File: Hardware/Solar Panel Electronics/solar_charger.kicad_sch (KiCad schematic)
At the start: 30 parts, among them J1 Screw_Terminal_SolarPanel_Inp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, U3 LT3652EDD, U4 LTC4411ES5TRMPBF

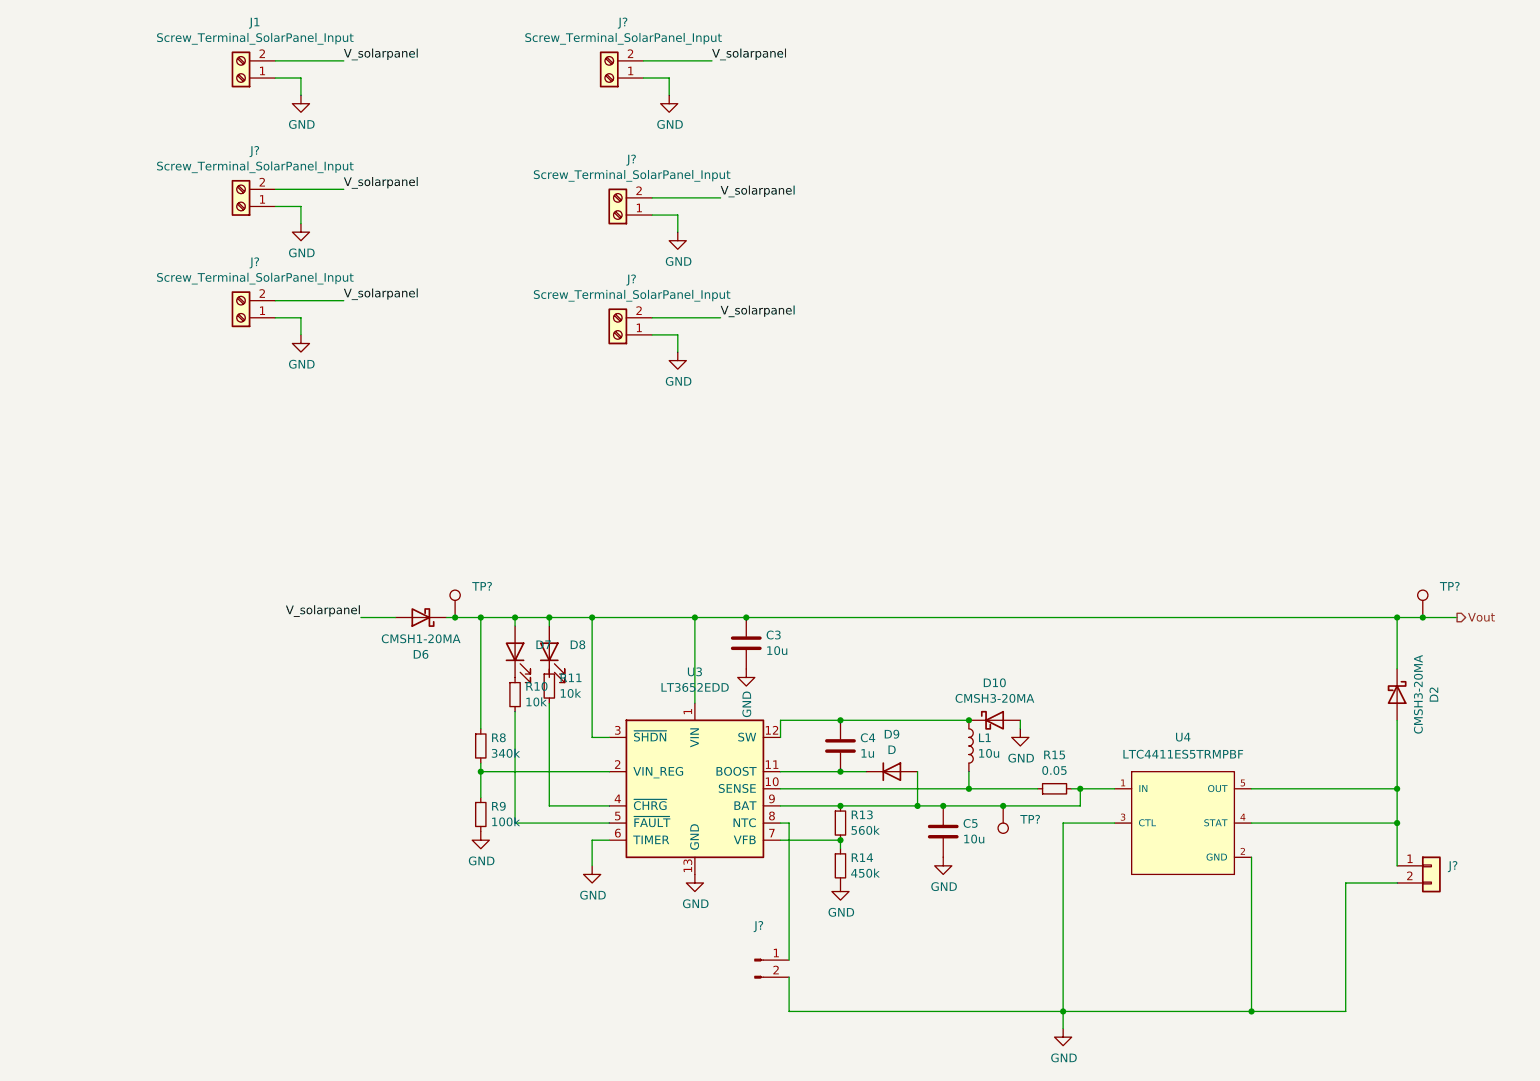
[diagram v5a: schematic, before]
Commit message: Added power measuring circuitry using potential dividers. Needs to be double checked
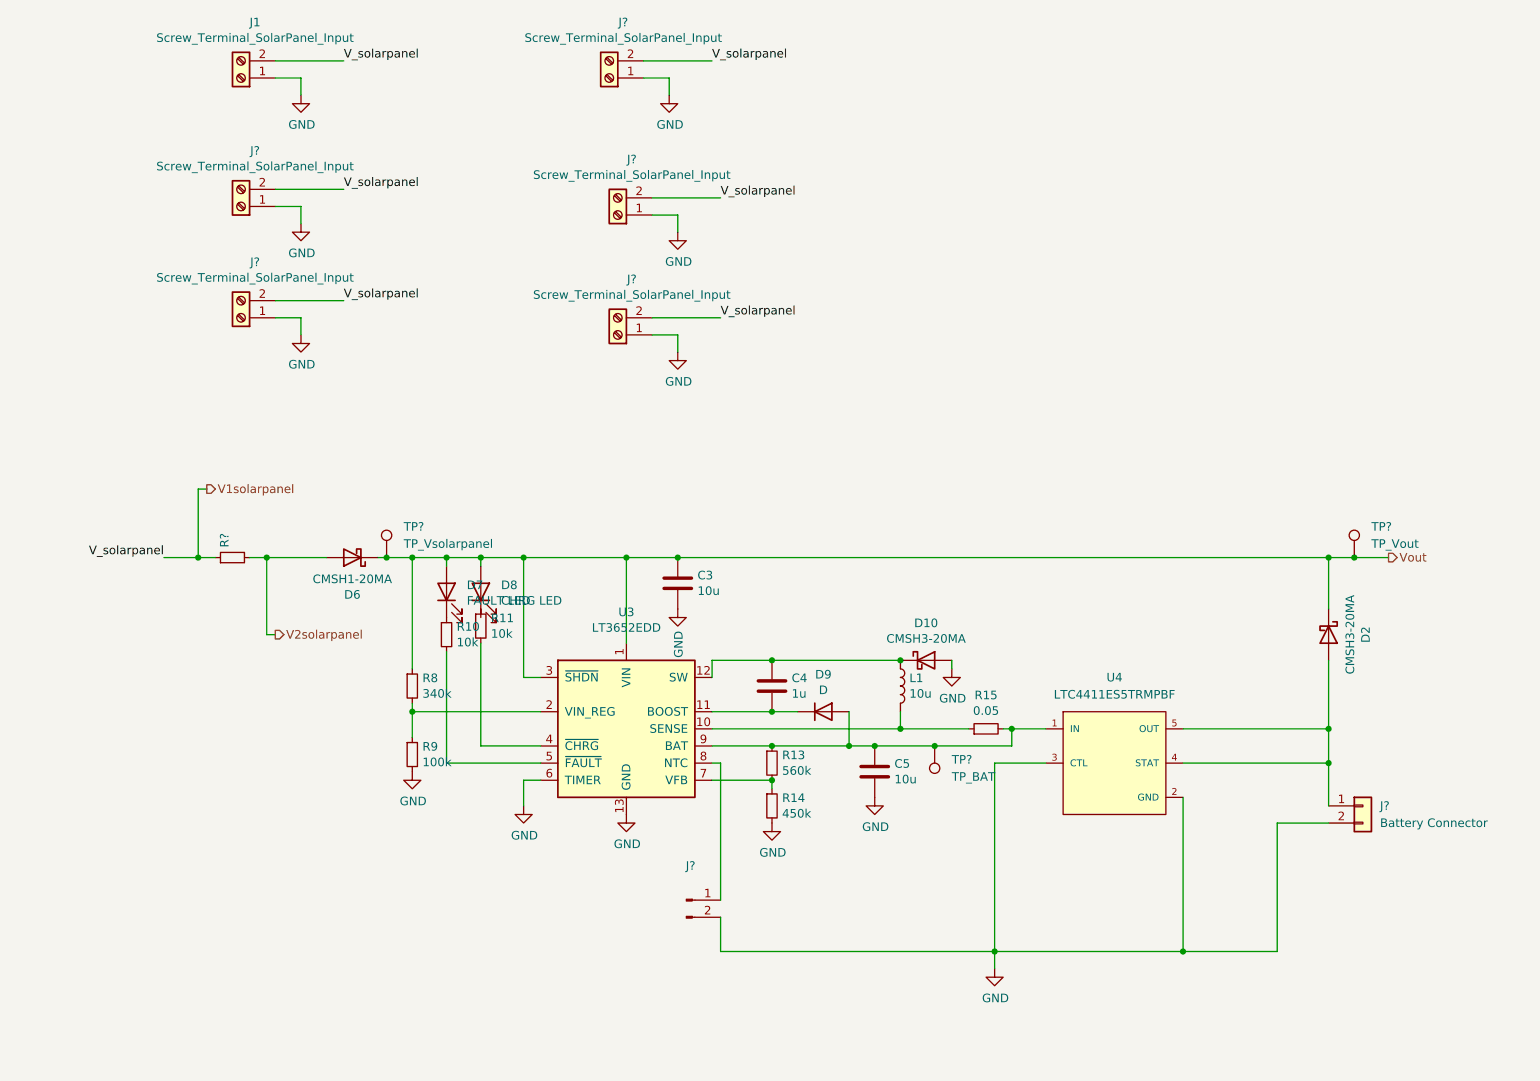
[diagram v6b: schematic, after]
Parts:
- added R?: (no value), symbol Device:R_Small
- D7: value (none) -> FAULT LED
- D8: value (none) -> CHRG LED
- J?: value (none) -> Battery Connector; footprint (none) -> Connector_JST:JST_ACH_BM02B-ACHSS-GAN-ETF_1x02-1MP_P1.20mm_Vertical
- TP?: value (none) -> TP_BAT
- TP?: value (none) -> TP_Vout
- TP?: value (none) -> TP_Vsolarpanel
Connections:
- net V_solarpanel renamed V1solarpanel
- net V1solarpanel: now also R?.1; no longer D6.2 (A)
- new net V2solarpanel: D6.2 (A), R?.2
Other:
- moved on the sheet: C3, C4, C5, D10, D2, D6, D7, D8, D9, J?, L1, R10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

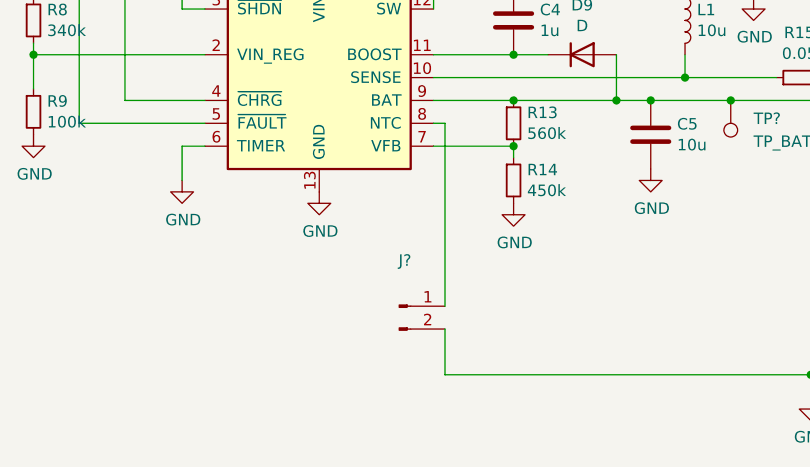
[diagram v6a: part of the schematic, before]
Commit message: Added voltage regulators. Need to size components
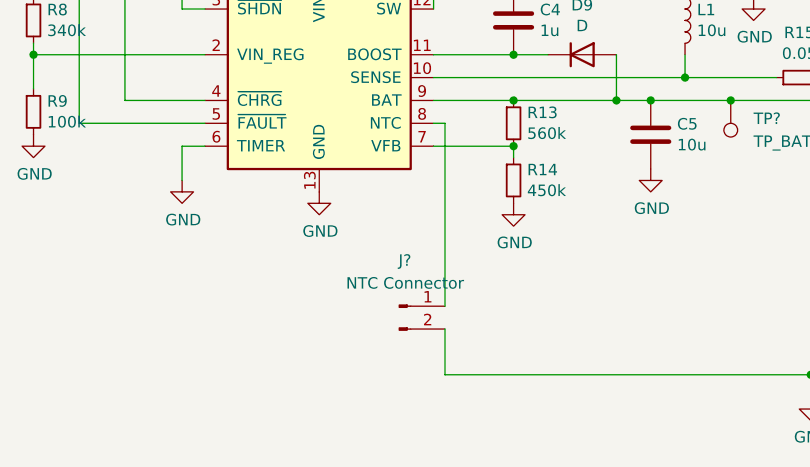
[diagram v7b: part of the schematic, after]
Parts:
- J?: value (none) -> NTC Connector
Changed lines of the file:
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@@
     (in_bom yes) (on_board yes) (fields_autoplaced)
     (property "Reference" "J?" (id 0) (at 114.935 140.97 0))
-    (property "Value" "" (id 1) (at 114.935 143.51 0))
+    (property "Value" "NTC Connector" (id 1) (at 114.935 143.51 0))
     (property "Footprint" "" (id 2) (at 114.3 146.05 0)
       (effects (font (size 1.27 1.27)) hide)

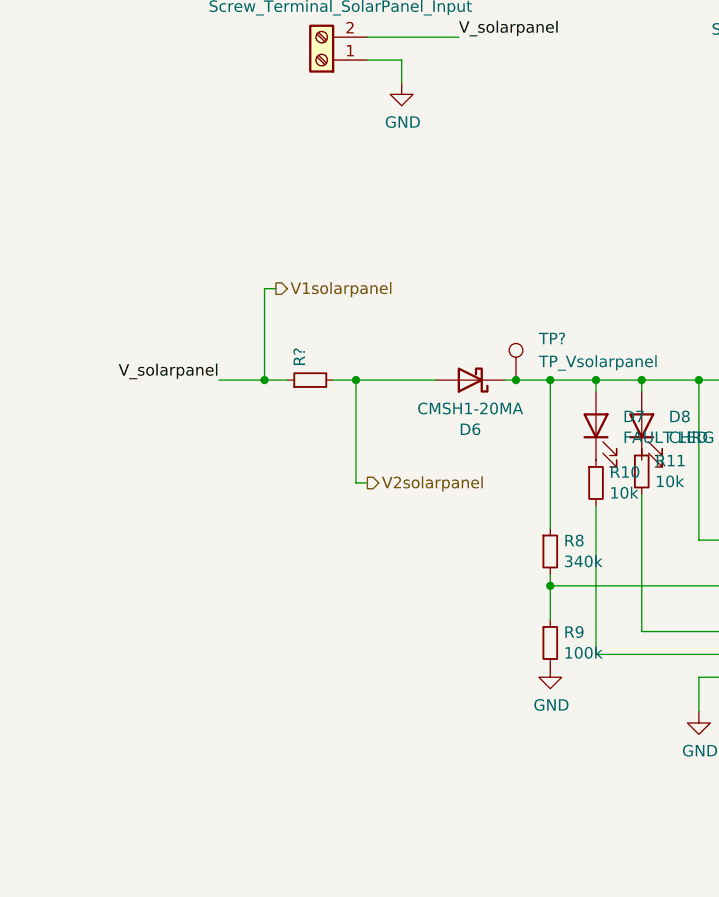
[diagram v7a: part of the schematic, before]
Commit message: Changed to use ADS131M04 adc instead of esp32 adc for power calculation
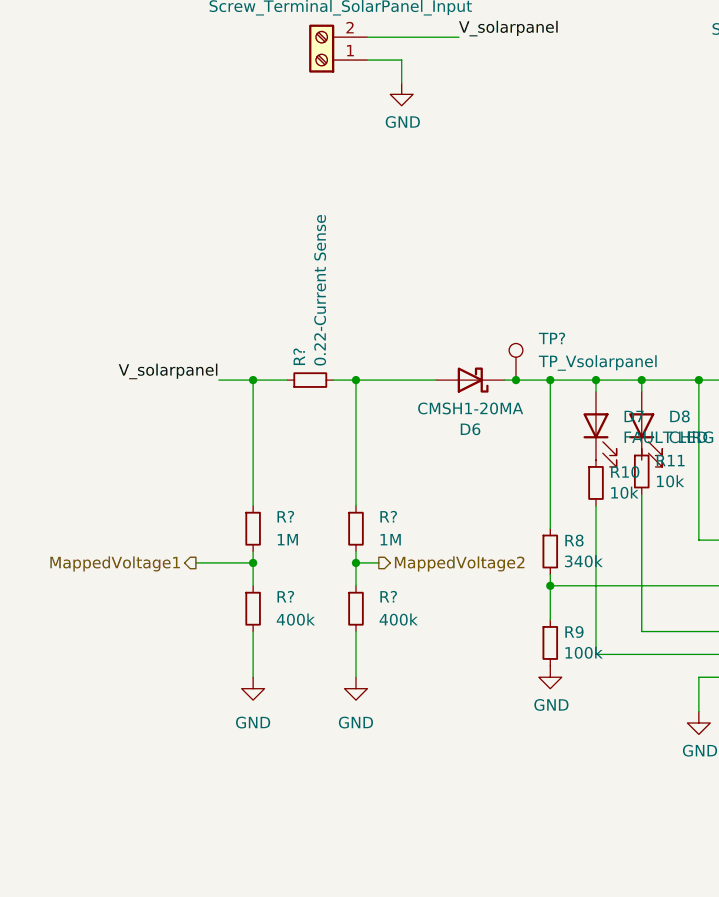
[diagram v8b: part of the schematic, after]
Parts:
- added R? (x2): 1M, symbol Device:R_Small
- added R? (x2): 400k, symbol Device:R_Small
- R?: value (none) -> 0.22-Current Sense
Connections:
- net GND: now also R?.2, R?.2
- net V1solarpanel renamed V_solarpanel
- net V_solarpanel: now also R?.1
- net V2solarpanel: no longer names the net of D6.2 (A), R?.2
- net V2solarpanel: now also R?.1
- new net MappedVoltage1: R?.1, R?.2
- new net MappedVoltage2: R?.1, R?.2
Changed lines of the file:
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@@
   (junction (at 146.05 120.65) (diameter 0) (color 0 0 0 0)
   )
+  (junction (at 52.07 115.57) (diameter 0) (color 0 0 0 0)
+  )
   (junction (at 127 110.49) (diameter 0) (color 0 0 0 0)
   )
@@
   (junction (at 209.55 95.25) (diameter 0) (color 0 0 0 0)
   )
+  (junction (at 40.64 115.57) (diameter 0) (color 0 0 0 0)
+  )
   (junction (at 127 128.27) (diameter 0) (color 0 0 0 0)
   )
@@
   (junction (at 113.03 95.25) (diameter 0) (color 0 0 0 0)
   )
-  (junction (at 41.91 95.25) (diameter 0) (color 0 0 0 0)
+  (junction (at 40.64 95.25) (diameter 0) (color 0 0 0 0)
   )
   (junction (at 127 118.11) (diameter 0) (color 0 0 0 0)
@@
     (stroke (width 0) (type default) (color 0 0 0 0))
   )
-  (wire (pts (xy 52.07 106.68) (xy 53.34 106.68))
-    (stroke (width 0) (type default) (color 0 0 0 0))
-  )
   (wire (pts (xy 209.55 110.49) (xy 209.55 120.65))
     (stroke (width 0) (type default) (color 0 0 0 0))
@@
     (stroke (width 0) (type default) (color 0 0 0 0))
   )
-  (wire (pts (xy 52.07 95.25) (xy 52.07 106.68))
+  (wire (pts (xy 52.07 95.25) (xy 52.07 109.22))
     (stroke (width 0) (type default) (color 0 0 0 0))
   )
@@
     (stroke (width 0) (type default) (color 0 0 0 0))
   )
-  (wire (pts (xy 41.91 85.09) (xy 43.18 85.09))
+  (wire (pts (xy 40.64 115.57) (xy 40.64 118.11))
     (stroke (width 0) (type default) (color 0 0 0 0))
   )
@@
     (stroke (width 0) (type default) (color 0 0 0 0))
   )
+  (wire (pts (xy 52.07 123.19) (xy 52.07 128.27))
+    (stroke (width 0) (type default) (color 0 0 0 0))
+  )
   (wire (pts (xy 83.82 123.19) (xy 92.71 123.19))
     (stroke (width 0) (type default) (color 0 0 0 0))
@@
     (stroke (width 0) (type default) (color 0 0 0 0))
   )
-  (wire (pts (xy 41.91 95.25) (xy 44.45 95.25))
+  (wire (pts (xy 36.83 95.25) (xy 40.64 95.25))
     (stroke (width 0) (type default) (color 0 0 0 0))
   )
@@
     (stroke (width 0) (type default) (color 0 0 0 0))
   )
+  (wire (pts (xy 52.07 114.3) (xy 52.07 115.57))
+    (stroke (width 0) (type default) (color 0 0 0 0))
+  )
   (wire (pts (xy 187.96 120.65) (xy 209.55 120.65))
     (stroke (width 0) (type default) (color 0 0 0 0))
@@
     (stroke (width 0) (type default) (color 0 0 0 0))
   )
+  (wire (pts (xy 40.64 114.3) (xy 40.64 115.57))
+    (stroke (width 0) (type default) (color 0 0 0 0))
+  )
   (wire (pts (xy 118.11 113.03) (xy 118.11 110.49))
     (stroke (width 0) (type default) (color 0 0 0 0))
@@
     (stroke (width 0) (type default) (color 0 0 0 0))
   )
-  (wire (pts (xy 36.83 95.25) (xy 41.91 95.25))
+  (wire (pts (xy 40.64 95.25) (xy 40.64 109.22))
     (stroke (width 0) (type default) (color 0 0 0 0))
   )
@@
     (stroke (width 0) (type default) (color 0 0 0 0))
   )
+  (wire (pts (xy 54.61 115.57) (xy 52.07 115.57))
+    (stroke (width 0) (type default) (color 0 0 0 0))
+  )
   (wire (pts (xy 73.66 118.11) (xy 92.71 118.11))
     (stroke (width 0) (type default) (color 0 0 0 0))
@@
     (stroke (width 0) (type default) (color 0 0 0 0))
   )
+  (wire (pts (xy 40.64 123.19) (xy 40.64 128.27))
+    (stroke (width 0) (type default) (color 0 0 0 0))
+  )
   (wire (pts (xy 119.38 148.59) (xy 119.38 153.67))
     (stroke (width 0) (type default) (color 0 0 0 0))
@@
     (stroke (width 0) (type default) (color 0 0 0 0))
   )
+  (wire (pts (xy 34.29 115.57) (xy 40.64 115.57))
+    (stroke (width 0) (type default) (color 0 0 0 0))
+  )
   (wire (pts (xy 109.22 41.91) (xy 119.38 41.91))
     (stroke (width 0) (type default) (color 0 0 0 0))
@@
     (stroke (width 0) (type default) (color 0 0 0 0))
   )
+  (wire (pts (xy 52.07 115.57) (xy 52.07 118.11))
+    (stroke (width 0) (type default) (color 0 0 0 0))
+  )
   (wire (pts (xy 127 110.49) (xy 146.05 110.49))
     (stroke (width 0) (type default) (color 0 0 0 0))
@@
     (stroke (width 0) (type default) (color 0 0 0 0))
   )
+  (wire (pts (xy 40.64 95.25) (xy 44.45 95.25))
+    (stroke (width 0) (type default) (color 0 0 0 0))
+  )
   (wire (pts (xy 78.74 125.73) (xy 92.71 125.73))
     (stroke (width 0) (type default) (color 0 0 0 0))
@@
   )
   (wire (pts (xy 127 128.27) (xy 127 129.54))
-    (stroke (width 0) (type default) (color 0 0 0 0))
-  )
-  (wire (pts (xy 41.91 95.25) (xy 41.91 85.09))
     (stroke (width 0) (type default) (color 0 0 0 0))
   )
@@
     (effects (font (size 1.27 1.27)) (justify left bottom))
   )
-  (hierarchical_label "V2solarpanel" (shape output) (at 53.34 106.68 0)
+  (hierarchical_label "MappedVoltage1" (shape output) (at 34.29 115.57 180)
+    (effects (font (size 1.27 1.27)) (justify right))
+  )
+  (hierarchical_label "Vout" (shape output) (at 218.44 95.25 0)
     (effects (font (size 1.27 1.27)) (justify left))
   )
-  (hierarchical_label "V1solarpanel" (shape output) (at 43.18 85.09 0)
-    (effects (font (size 1.27 1.27)) (justify left))
-  )
-  (hierarchical_label "Vout" (shape output) (at 218.44 95.25 0)
+  (hierarchical_label "MappedVoltage2" (shape output) (at 54.61 115.57 0)
     (effects (font (size 1.27 1.27)) (justify left))
   )
@@
     (pin "2")
   )
+  (symbol (lib_id "power:GND") (at 52.07 128.27 0) (unit 1)
+    (in_bom yes) (on_board yes) (fields_autoplaced)
+    (property "Reference" "#PWR?" (id 0) (at 52.07 134.62 0)
+      (effects (font (size 1.27 1.27)) hide)
+    )
+    (property "Value" "GND" (id 1) (at 52.07 133.35 0))
+    (property "Footprint" "" (id 2) (at 52.07 128.27 0)
+      (effects (font (size 1.27 1.27)) hide)
+    )
+    (property "Datasheet" "" (id 3) (at 52.07 128.27 0)
+      (effects (font (size 1.27 1.27)) hide)
+    )
+    (pin "1")
+  )
   (symbol (lib_id "Connector:Screw_Terminal_01x02") (at 48.26 43.18 180) (unit 1)
     (in_bom yes) (on_board yes)
@@
     (pin "1")
   )
+  (symbol (lib_id "Device:R_Small") (at 52.07 111.76 0) (unit 1)
+    (in_bom yes) (on_board yes) (fields_autoplaced)
+    (property "Reference" "R?" (id 0) (at 54.61 110.4899 0)
+      (effects (font (size 1.27 1.27)) (justify left))
+    )
+    (property "Value" "1M" (id 1) (at 54.61 113.0299 0)
+      (effects (font (size 1.27 1.27)) (justify left))
+    )
+    (property "Footprint" "" (id 2) (at 52.07 111.76 0)
+      (effects (font (size 1.27 1.27)) hide)
+    )
+    (property "Datasheet" "~" (id 3) (at 52.07 111.76 0)
+      (effects (font (size 1.27 1.27)) hide)
+    )
+    (pin "1")
+    (pin "2")
+  )
   (symbol (lib_id "power:GND") (at 57.15 62.23 0) (unit 1)
     (in_bom yes) (on_board yes)
@@
     (pin "2")
   )
+  (symbol (lib_id "Device:R_Small") (at 40.64 111.76 0) (unit 1)
+    (in_bom yes) (on_board yes) (fields_autoplaced)
+    (property "Reference" "R?" (id 0) (at 43.18 110.4899 0)
+      (effects (font (size 1.27 1.27)) (justify left))
+    )
+    (property "Value" "1M" (id 1) (at 43.18 113.0299 0)
+      (effects (font (size 1.27 1.27)) (justify left))
+    )
+    (property "Footprint" "" (id 2) (at 40.64 111.76 0)
+      (effects (font (size 1.27 1.27)) hide)
+    )
+    (property "Datasheet" "~" (id 3) (at 40.64 111.76 0)
+      (effects (font (size 1.27 1.27)) hide)
+    )
+    (pin "1")
+    (pin "2")
+  )
   (symbol (lib_id "power:GND") (at 57.15 45.72 0) (unit 1)
     (in_bom yes) (on_board yes)
@@
       (effects (font (size 1.27 1.27)) (justify left))
     )
-    (property "Value" "" (id 1) (at 48.133 93.7514 0)
+    (property "Value" "0.22-Current Sense" (id 1) (at 48.133 93.7514 0)
       (effects (font (size 1.27 1.27)) (justify left))
     )
@@
     (pin "2")
   )
+  (symbol (lib_id "Device:R_Small") (at 52.07 120.65 0) (unit 1)
+    (in_bom yes) (on_board yes) (fields_autoplaced)
+    (property "Reference" "R?" (id 0) (at 54.61 119.3799 0)
+      (effects (font (size 1.27 1.27)) (justify left))
+    )
+    (property "Value" "400k" (id 1) (at 54.61 121.9199 0)
+      (effects (font (size 1.27 1.27)) (justify left))
+    )
+    (property "Footprint" "" (id 2) (at 52.07 120.65 0)
+      (effects (font (size 1.27 1.27)) hide)
+    )
+    (property "Datasheet" "~" (id 3) (at 52.07 120.65 0)
+      (effects (font (size 1.27 1.27)) hide)
+    )
+    (pin "1")
+    (pin "2")
+  )
   (symbol (lib_id "Connector_Generic:Conn_01x02") (at 214.63 132.08 0) (unit 1)
     (in_bom yes) (on_board yes) (fields_autoplaced)
@@
     )
     (property "Datasheet" "~" (id 3) (at 218.44 95.25 0)
+      (effects (font (size 1.27 1.27)) hide)
+    )
+    (pin "1")
+  )
+  (symbol (lib_id "power:GND") (at 40.64 128.27 0) (unit 1)
+    (in_bom yes) (on_board yes) (fields_autoplaced)
+    (property "Reference" "#PWR?" (id 0) (at 40.64 134.62 0)
+      (effects (font (size 1.27 1.27)) hide)
+    )
+    (property "Value" "GND" (id 1) (at 40.64 133.35 0))
+    (property "Footprint" "" (id 2) (at 40.64 128.27 0)
+      (effects (font (size 1.27 1.27)) hide)
+    )
+    (property "Datasheet" "" (id 3) (at 40.64 128.27 0)
       (effects (font (size 1.27 1.27)) hide)
     )
@@
     (pin "5")
   )
+  (symbol (lib_id "Device:R_Small") (at 40.64 120.65 0) (unit 1)
+    (in_bom yes) (on_board yes) (fields_autoplaced)
+    (property "Reference" "R?" (id 0) (at 43.18 119.3799 0)
+      (effects (font (size 1.27 1.27)) (justify left))
+    )
+    (property "Value" "400k" (id 1) (at 43.18 121.9199 0)
+      (effects (font (size 1.27 1.27)) (justify left))
+    )
+    (property "Footprint" "" (id 2) (at 40.64 120.65 0)
+      (effects (font (size 1.27 1.27)) hide)
+    )
+    (property "Datasheet" "~" (id 3) (at 40.64 120.65 0)
+      (effects (font (size 1.27 1.27)) hide)
+    )
+    (pin "1")
+    (pin "2")
+  )
 )
